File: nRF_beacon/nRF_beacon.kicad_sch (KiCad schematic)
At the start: 5 parts, among them J1 USB_C_Receptacle_PowerOnly_6P, J2 Conn_01x03

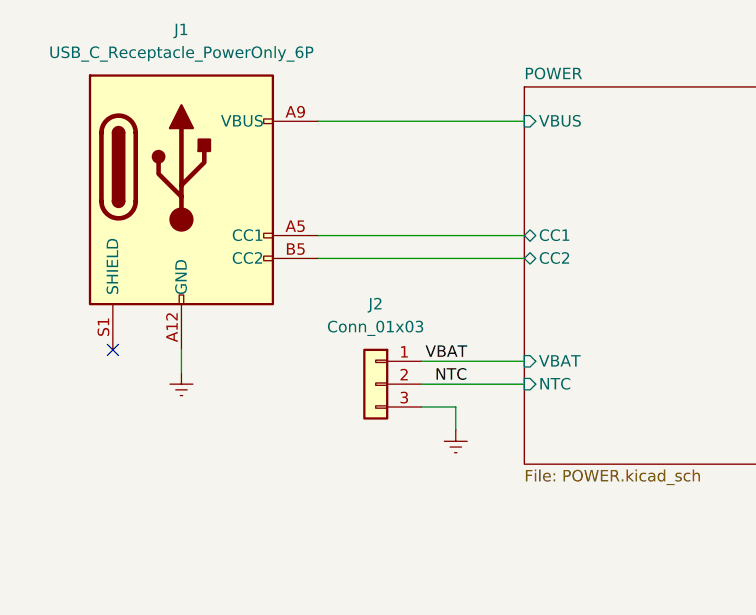
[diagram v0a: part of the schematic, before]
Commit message: Added buck configuration for AUDIO 3.3V power. Removed USB input
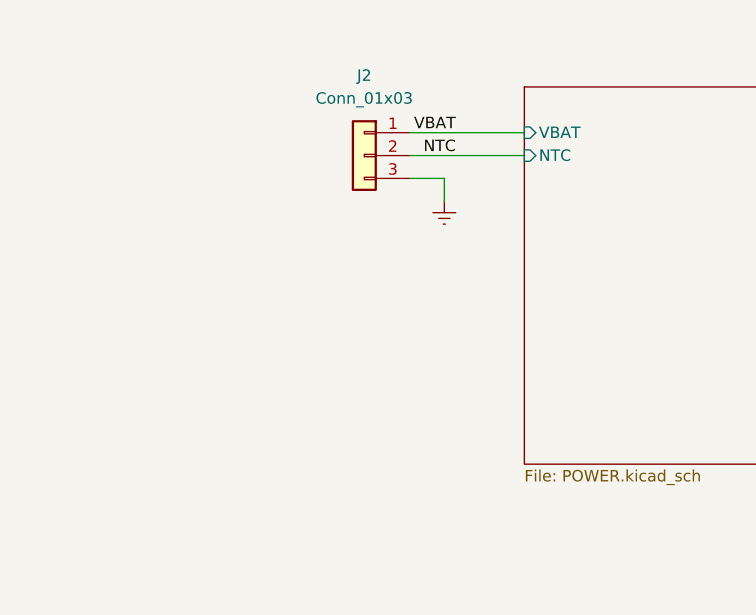
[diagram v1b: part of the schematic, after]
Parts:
- removed J1: USB_C_Receptacle_PowerOnly_6P, symbol Connector:USB_C_Receptacle_PowerOnly_6P
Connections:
- no-connect marks 1 -> 0
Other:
- sheet POWER ports: added none; removed CC1, CC2, VBUS
- moved on the sheet: J2

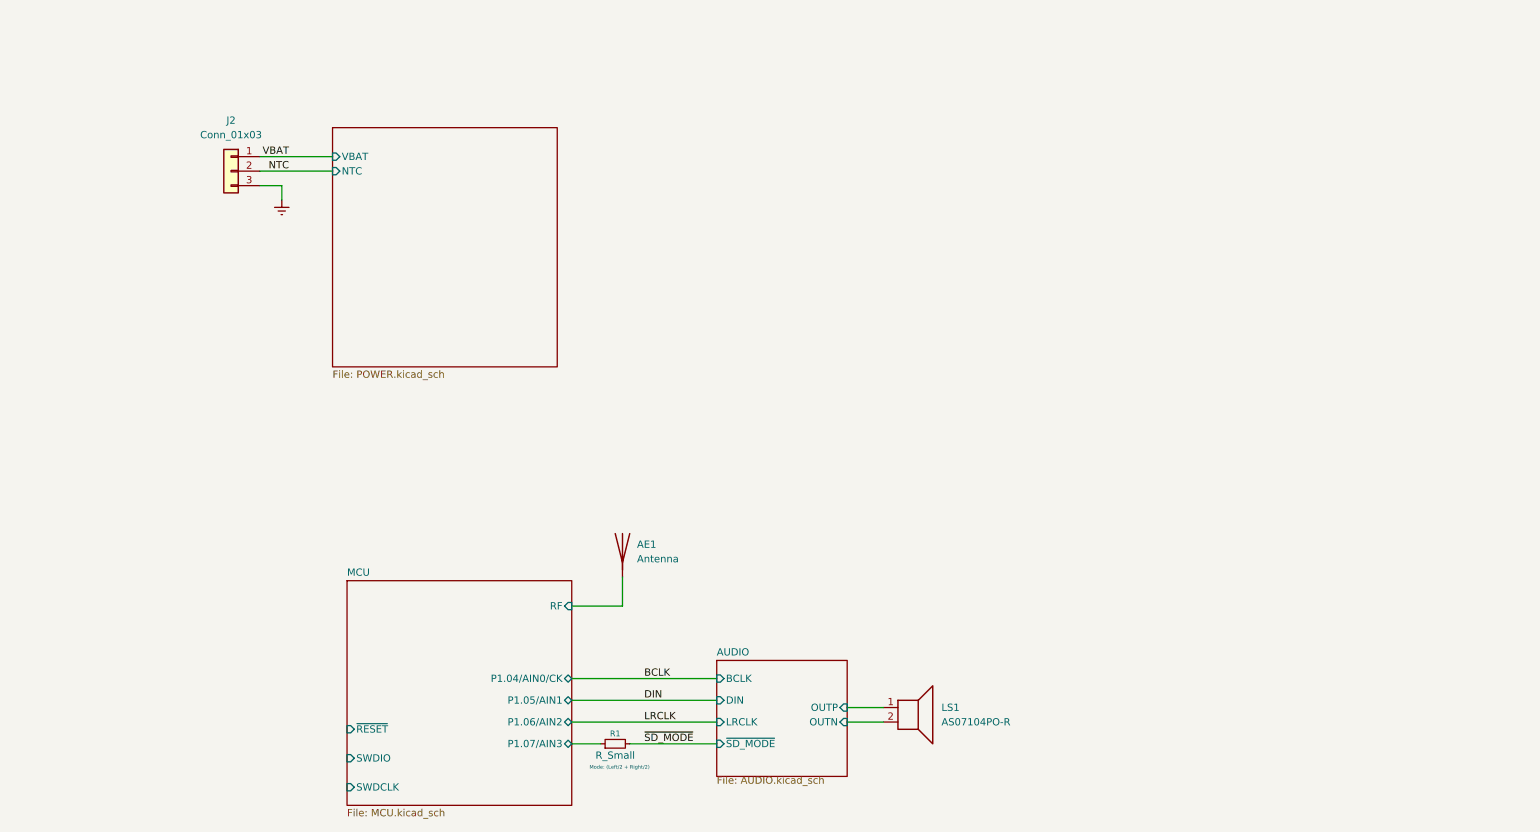
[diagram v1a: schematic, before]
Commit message: Updated nPM schematic. Added TWI and debug connector
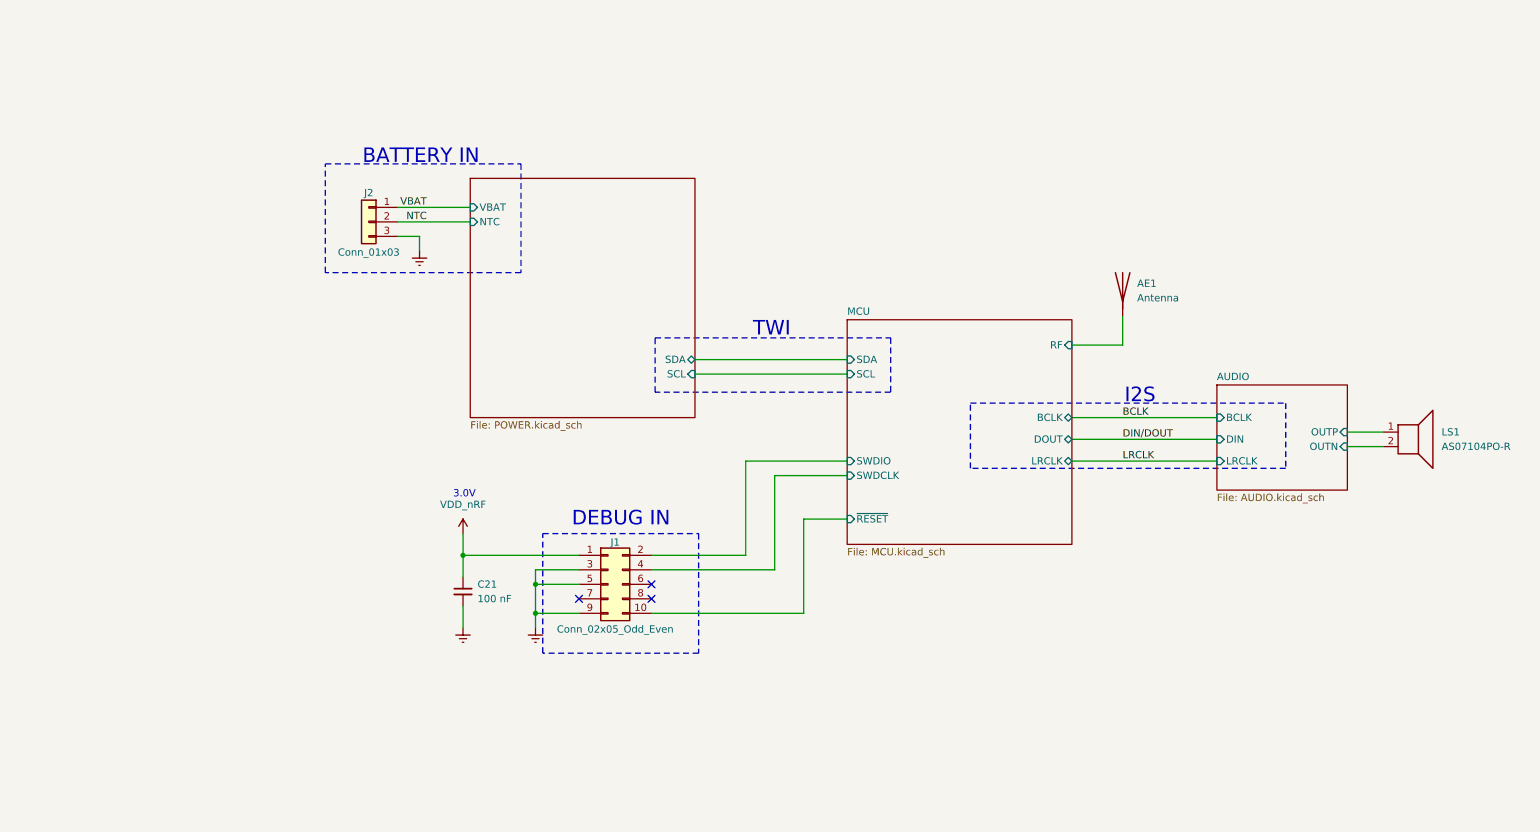
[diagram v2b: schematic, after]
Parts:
- removed R1: R_Small, symbol Device:R_Small
- added C21: 100 nF, symbol Device:C_Small
- added J1: Conn_02x05_Odd_Even, symbol Connector_Generic:Conn_02x05_Odd_Even
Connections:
- net Earth: now also C21.2, J1.3 (Pin_3), J1.5 (Pin_5), J1.9 (Pin_9)
- net MCU/SWDCLK: now also J1.4 (Pin_4)
- net MCU/SWDIO: now also J1.2 (Pin_2)
- net MCU/~{RESET}: now also J1.10 (Pin_10)
- new net VDD_nRF: C21.1, J1.1 (Pin_1)
- no-connect marks 0 -> 3
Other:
- sheet AUDIO ports: added none; removed ~{SD_MODE}
- sheet MCU ports: added BCLK, DOUT, LRCLK, SCL, SDA; removed P1.04/AIN0/CK, P1.05/AIN1, P1.06/AIN2, P1.07/AIN3
- sheet POWER ports: added SCL, SDA; removed none
- note added: "3.0V"
- note added: "BATTERY IN"
- note added: "DEBUG IN"
- note added: "I2S"
- note added: "TWI"
- note removed: "Mode: (Left/2 + Right/2)"
- moved on the sheet: AE1, J2, LS1

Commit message: Added LEDs and BUCK supply from VSYS
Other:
- note added: "MAX98357A"
- note added: "nPM1300"
- note added: "nRF54L15"
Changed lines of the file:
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@@
+		)
+	)
+	(text "nPM1300"
+		(exclude_from_sim no)
+		(at 113.538 43.434 0)
+		(effects
+			(font
+				(size 2.54 2.54)
+			)
 		)
 	)
@@
 		)
 	)
+	(text "nRF54L15"
+		(exclude_from_sim no)
+		(at 178.816 68.58 0)
+		(effects
+			(font
+				(size 2.54 2.54)
+			)
+		)
+	)
 	(text "TWI"
 		(exclude_from_sim no)
@@
 		(effects
 			(font
+				(size 2.54 2.54)
+			)
+		)
+	)
+	(text "MAX98357A"
+		(exclude_from_sim no)
+		(at 236.22 78.486 0)
+		(effects
+			(font

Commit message: Finished first schematic draft. Ready for layout
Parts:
- removed J2: Conn_01x03, symbol Connector_Generic:Conn_01x03
- added J2: Conn_02x03_Counter_Clockwise, Ekse:SAMTEC_TSM-103-01-L-DV-P-TR, symbol Connector_Generic:Conn_02x03_Counter_Clockwise
- added U4: 12BHC186P1-GR, Ekse:12BHC186P1GR, symbol Ekse:12BHC186P1-GR
- AE1: footprint (none) -> Ekse:PCB_Antenna
- C21: value 100 nF -> 0.1uF; footprint (none) -> Capacitor_SMD:C_0201_0603Metric_Pad0.64x0.40mm_HandSolder; MPN (none) -> KGM03BR51E104KH; Price (none) -> 1.39
- J1: footprint (none) -> Ekse:FTSH-105-XX-YYY-DV-K-P-TR; MPN (none) -> FTSH-105-01-F-DV-K-P; Price (none) -> 21
- LS1: footprint (none) -> Ekse:VN02A1500000G; MPN (none) -> AS07104PO-R; Price (none) -> 47.21
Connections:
- net Earth: now also U4.2
- net VBAT: now also U4.1
- new net P1.07: J2.5 (Pin_5)
- new net P1.08: J2.6 (Pin_6)
- new net P1.09: J2.1 (Pin_1)
- new net P1.10: J2.2 (Pin_2)
- new net P1.13: J2.3 (Pin_3)
- new net P1.14: J2.4 (Pin_4)
- no-connect marks 3 -> 5
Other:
- sheet MCU ports: added P1.07, P1.08, P1.09, P1.10, P1.13, P1.14; removed none
- sheet POWER ports: added none; removed NTC
- note added: "GPIO"

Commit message: Began matching network layout
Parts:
- C21: footprint Capacitor_SMD:C_0201_0603Metric_Pad0.64x0.40mm_HandSolder -> Capacitor_SMD:C_0201_0603Metric
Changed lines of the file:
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@@
 			)
 		)
-		(property "Footprint" "Capacitor_SMD:C_0201_0603Metric_Pad0.64x0.40mm_HandSolder"
+		(property "Footprint" "Capacitor_SMD:C_0201_0603Metric"
 			(at 92.71 118.11 0)
 			(effects

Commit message: Added most of the components to nRF54 typical application layout
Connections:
- net Earth renamed GND
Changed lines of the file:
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@@
 			)
 		)
-		(property "Value" "Earth"
+		(property "Value" "GND"
 			(at 82.55 64.77 0)
 			(effects
@@
 			)
 		)
-		(property "Description" "Power symbol creates a global label with name \"Earth\""
+		(property "Description" "Power symbol creates a global label with name \"GND\""
 			(at 82.55 59.69 0)
 			(effects
@@
 			)
 		)
-		(property "Value" "Earth"
+		(property "Value" "GND"
 			(at 105.41 129.54 0)
 			(effects
@@
 			)
 		)
-		(property "Description" "Power symbol creates a global label with name \"Earth\""
+		(property "Description" "Power symbol creates a global label with name \"GND\""
 			(at 105.41 124.46 0)
 			(effects
@@
 			)
 		)
-		(property "Value" "Earth"
+		(property "Value" "GND"
 			(at 92.71 129.54 0)
 			(effects
@@
 			)
 		)
-		(property "Description" "Power symbol creates a global label with name \"Earth\""
+		(property "Description" "Power symbol creates a global label with name \"GND\""
 			(at 92.71 124.46 0)
 			(effects

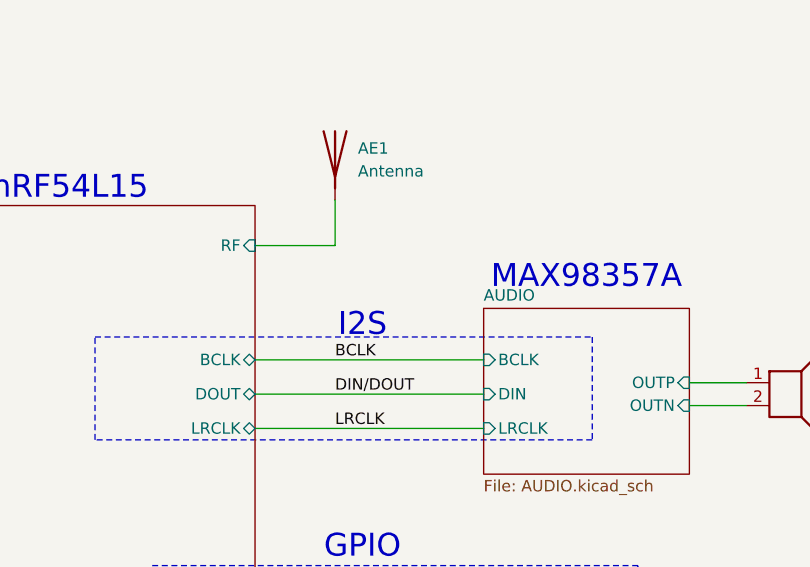
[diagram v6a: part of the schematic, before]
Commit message: Added transmission line, and new folder for report screenshots
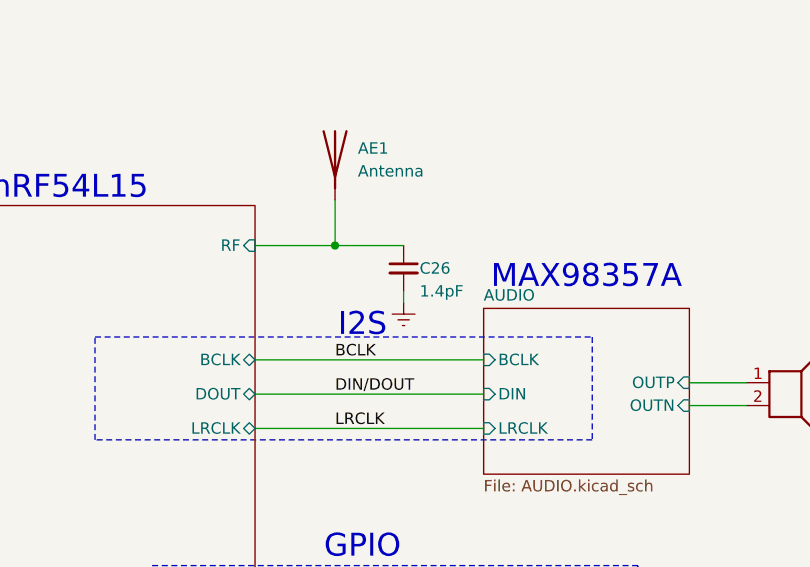
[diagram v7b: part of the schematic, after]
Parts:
- added C26: 1.4pF, Capacitor_SMD:C_0201_0603Metric, symbol Device:C_Small
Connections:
- net GND: now also C26.2
- net MCU/RF: now also C26.1
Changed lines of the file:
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@@
+	)
+	(junction
+		(at 208.28 74.93)
+		(diameter 0)
+		(color 0 0 0 0)
 	)
 	(junction
@@
 	(wire
 		(pts
+			(xy 215.9 80.01) (xy 215.9 81.28)
+		)
+		(stroke
+			(width 0)
+			(type default)
+		)
+	)
+	(wire
+		(pts
 			(xy 199.39 127) (xy 234.95 127)
 		)
@@
 		(pts
 			(xy 199.39 121.92) (xy 220.98 121.92)
+		)
+		(stroke
+			(width 0)
+			(type default)
+		)
+	)
+	(wire
+		(pts
+			(xy 208.28 74.93) (xy 215.9 74.93)
 		)
 		(stroke
@@
 			)
 			(justify left bottom)
+		)
+	)
+	(symbol
+		(lib_id "power:Earth")
+		(at 215.9 81.28 0)
+		(unit 1)
+		(exclude_from_sim no)
+		(in_bom yes)
+		(on_board yes)
+		(dnp no)
+		(fields_autoplaced yes)
+		(property "Reference" "#PWR043"
+			(at 215.9 87.63 0)
+			(effects
+				(font
+					(size 1.27 1.27)
+				)
+				(hide yes)
+			)
+		)
+		(property "Value" "GND"
+			(at 215.9 86.36 0)
+			(effects
+				(font
+					(size 1.27 1.27)
+				)
+				(hide yes)
+			)
+		)
+		(property "Footprint" ""
+			(at 215.9 81.28 0)
+			(effects
+				(font
+					(size 1.27 1.27)
+				)
+				(hide yes)
+			)
+		)
+		(property "Datasheet" "~"
+			(at 215.9 81.28 0)
+			(effects
+				(font
+					(size 1.27 1.27)
+				)
+				(hide yes)
+			)
+		)
+		(property "Description" "Power symbol creates a global label with name \"GND\""
+			(at 215.9 81.28 0)
+			(effects
+				(font
+					(size 1.27 1.27)
+				)
+				(hide yes)
+			)
+		)
+		(pin "1"
+		)
+		(instances
+			(project "nRF_beacon"
+				(path "/1290e5f5-b91f-4d6e-b440-6b78e8fdc212"
+					(reference "#PWR043")
+					(unit 1)
+				)
+			)
 		)
 	)
@@
 					(unit 1)
 				)
+			)
+		)
+	)
+	(symbol
+		(lib_id "Device:C_Small")
+		(at 215.9 77.47 0)
+		(unit 1)
+		(exclude_from_sim no)
+		(in_bom yes)
+		(on_board yes)
+		(dnp no)
+		(property "Reference" "C26"
+			(at 217.678 77.47 0)
+			(effects
+				(font
+					(size 1.27 1.27)
+				)
+				(justify left)
+			)
+		)
+		(property "Value" "1.4pF"
+			(at 217.678 80.01 0)
+			(effects
+				(font
+					(size 1.27 1.27)
+				)
+				(justify left)
+			)
+		)
+		(property "Footprint" "Capacitor_SMD:C_0201_0603Metric"
+			(at 215.9 77.47 0)
+			(effects
+				(font
+					(size 1.27 1.27)
+				)
+				(hide yes)
+			)
+		)
+		(property "Datasheet" "~"
+			(at 215.9 77.47 0)
+			(effects
+				(font
+					(size 1.27 1.27)
+				)
+				(hide yes)
+			)
+		)
+		(property "Description" "Unpolarized capacitor, small symbol"
+			(at 215.9 77.47 0)
+			(effects
+				(font
+					(size 1.27 1.27)
+				)
+				(hide yes)
+			)
+		)
+		(pin "1"
+		)
+		(pin "2"
+		)
+		(instances
+			(project ""
+				(path "/1290e5f5-b91f-4d6e-b440-6b78e8fdc212"
+					(reference "C26")
+					(unit 1)
+				)

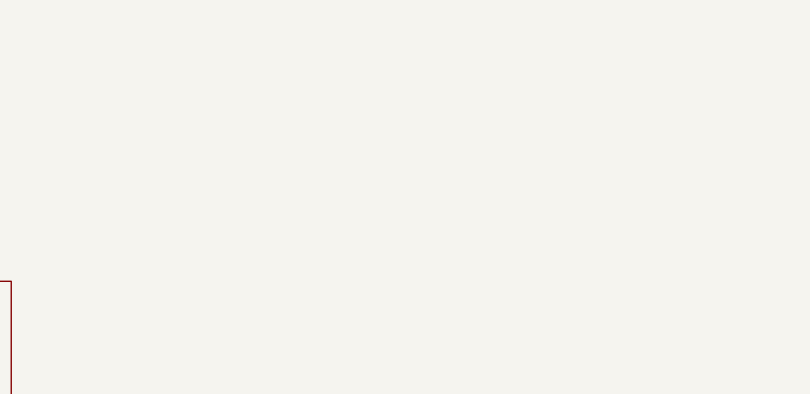
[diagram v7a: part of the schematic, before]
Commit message: Cleaned up silkscreen
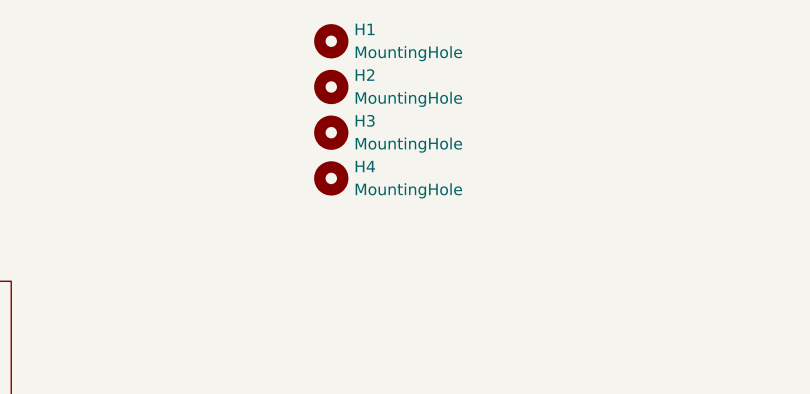
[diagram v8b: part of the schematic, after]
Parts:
- added H1, H2, H3, H4: MountingHole, MountingHole:MountingHole_3.2mm_M3, symbol Mechanical:MountingHole
